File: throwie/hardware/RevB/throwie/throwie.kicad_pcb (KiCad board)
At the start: 2 copper layers, 24 parts, among them J1 CONN, Q1 2SC3356, Q2 SS8050-G, T1 TestPoints, T2 TestPoints, T3 TestPoints, T4 TestPoints, U1 C8051F850-A-GU, U2 MIC5231-3.3YM5-TR, X1 RO3101

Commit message: final layout
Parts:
- moved A1 1.98 mm to (51.1, 145.5)
- moved R3 1.02 mm to (51.6, 158.5)
- moved C6 0.76 mm to (49.5, 158.5)
- moved C2 0.55 mm to (52.3, 153.4)
- moved R2 0.53 mm to (46.0, 158.5)
- moved T1 0.51 mm to (42.4, 161.0)
- moved T2 0.25 mm to (45.7, 161.0)
- moved T3 0.25 mm to (52.3, 161.0)
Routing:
- net GNDREF: track 106.0 -> 145.4 mm, vias 18 -> 36
- net +3V3: track 11.3 -> 37.5 mm, vias 1 -> 3
- net +BATT: track 34.0 -> 43.2 mm, vias 1 -> 3
- net Net-(R5-Pad2): track 24.4 -> 16.4 mm
- net Net-(T4-Pad1): track 11.0 -> 17.9 mm
- net Net-(A1-Pad1): track 12.7 -> 15.5 mm
- net /0.471: track 8.89 -> 7.79 mm
- net /MOD: track 28.4 -> 27.5 mm
- net Net-(C4-Pad1): track 29.6 -> 30.2 mm
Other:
- board outline added: 33.8 x 18.8 mm
- board text added: "1"
- board text added: "2"
- board text added: "3"
- board text added: "4"
- board text added: "AJR Nov 2021"

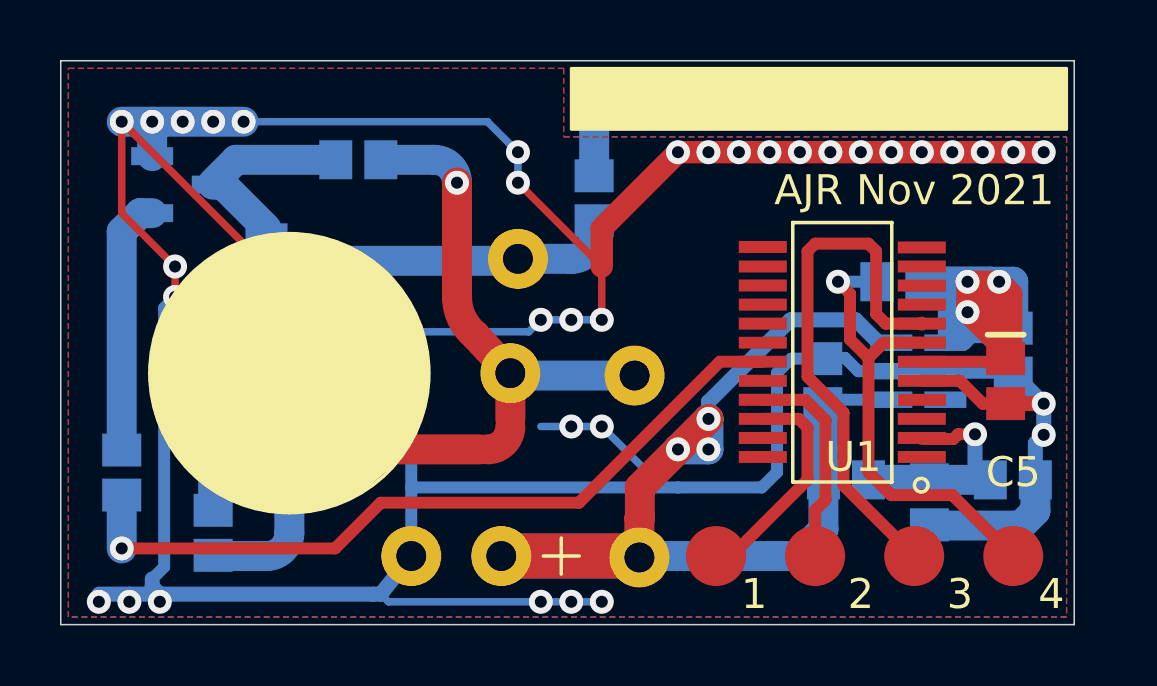
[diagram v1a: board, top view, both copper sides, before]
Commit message: more silk
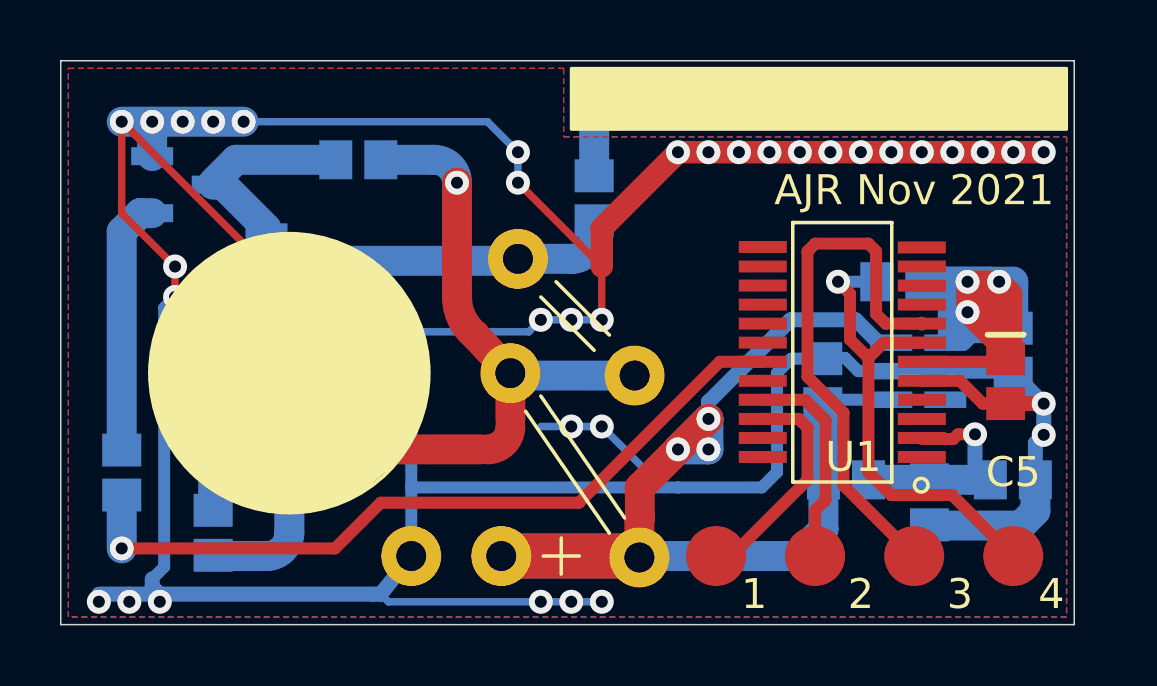
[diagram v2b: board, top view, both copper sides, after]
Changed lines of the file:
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@@
   (general
     (thickness 1.6)
-    (drawings 29)
+    (drawings 33)
     (tracks 275)
     (zones 0)
@@
     (32 B.Adhes user hide)
     (33 F.Adhes user hide)
-    (34 B.Paste user)
+    (34 B.Paste user hide)
     (35 F.Paste user hide)
-    (36 B.SilkS user)
+    (36 B.SilkS user hide)
     (37 F.SilkS user)
     (38 B.Mask user hide)
-    (39 F.Mask user)
+    (39 F.Mask user hide)
     (40 Dwgs.User user hide)
     (41 Cmts.User user hide)
@@
       (net 3 +BATT))
   )
+  (gr_line (start 36.576 152.4) (end 38.354 154.178) (layer F.SilkS) (width 0.12))
+  (gr_line (start 37.084 151.892) (end 38.862 153.67) (layer F.SilkS) (width 0.12))
+  (gr_line (start 36.576 155.702) (end 39.37 159.766) (layer F.SilkS) (width 0.12))
+  (gr_line (start 36.068 156.21) (end 38.862 160.274) (layer F.SilkS) (width 0.12))
   (gr_arc (start 34.798 156.718) (end 34.798 157.48) (angle -90) (layer F.Cu) (width 1))
   (gr_line (start 34.374421 153.664684) (end 35.56 154.94) (layer F.Cu) (width 1))
@@
   )
   (zone (net 2) (net_name GNDREF) (layer F.Cu) (hatch edge 0.508)
-    (connect_pads (clearance 0.254))
+    (connect_pads thru_hole_only (clearance 0.254))
     (min_thickness 0.254)
     (fill yes (arc_segments 32) (thermal_gap 0.508) (thermal_bridge_width 0.508))
@@
       )
     )
+  )
+  (zone (net 0) (net_name "") (layer F.Cu) (hatch edge 0.508)
+    (connect_pads thru_hole_only (clearance 0.254))
+    (min_thickness 0.254)
+    (keepout (tracks allowed) (vias allowed) (copperpour not_allowed))
+    (fill (arc_segments 32) (thermal_gap 0.508) (thermal_bridge_width 0.508))
+    (polygon
+      (pts
+        (xy 50.292 158.496) (xy 46.736 158.496) (xy 46.482 154.432) (xy 50.292 154.432)
+      )
+    )
+  )
+  (zone (net 0) (net_name "") (layer F.Cu) (hatch edge 0.508)
+    (connect_pads thru_hole_only (clearance 0.254))
+    (min_thickness 0.254)
+    (keepout (tracks allowed) (vias allowed) (copperpour not_allowed))
+    (fill (arc_segments 32) (thermal_gap 0.508) (thermal_bridge_width 0.508))
+    (polygon
+      (pts
+        (xy 52.832 161.29) (xy 41.148 161.29) (xy 41.402 159.258) (xy 50.292 159.004)
+      )
+    )
+  )
+  (zone (net 0) (net_name "") (layer B.Cu) (hatch edge 0.508)
+    (connect_pads thru_hole_only (clearance 0.254))
+    (min_thickness 0.254)
+    (keepout (tracks allowed) (vias allowed) (copperpour not_allowed))
+    (fill (arc_segments 32) (thermal_gap 0.508) (thermal_bridge_width 0.508))
+    (polygon
+      (pts
+        (xy 50.038 160.782) (xy 49.276 161.544) (xy 45.212 161.544) (xy 45.974 159.258) (xy 50.038 159.258)
+      )
+    )
+  )
+  (zone (net 0) (net_name "") (layer B.Cu) (hatch edge 0.508)
+    (connect_pads thru_hole_only (clearance 0.254))
+    (min_thickness 0.254)
+    (keepout (tracks allowed) (vias allowed) (copperpour not_allowed))
+    (fill (arc_segments 32) (thermal_gap 0.508) (thermal_bridge_width 0.508))
+    (polygon
+      (pts
+        (xy 51.562 155.702) (xy 52.832 155.702) (xy 52.832 157.988) (xy 51.054 157.988) (xy 51.054 155.448)
+        (xy 51.308 155.448)
+      )
+    )
+  )
+  (zone (net 0) (net_name "") (layer F.Cu) (hatch edge 0.508)
+    (connect_pads thru_hole_only (clearance 0.254))
+    (min_thickness 0.254)
+    (keepout (tracks allowed) (vias allowed) (copperpour not_allowed))
+    (fill (arc_segments 32) (thermal_gap 0.508) (thermal_bridge_width 0.508))
+    (polygon
+      (pts
+        (xy 34.29 161.798) (xy 33.528 161.798) (xy 33.528 161.29) (xy 29.972 161.29) (xy 29.972 160.528)
+        (xy 34.798 159.766)
+      )
+    )
